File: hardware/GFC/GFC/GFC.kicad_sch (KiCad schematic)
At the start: 11 parts, among them J1 BATCON, J2 Pi Zero/Zero W

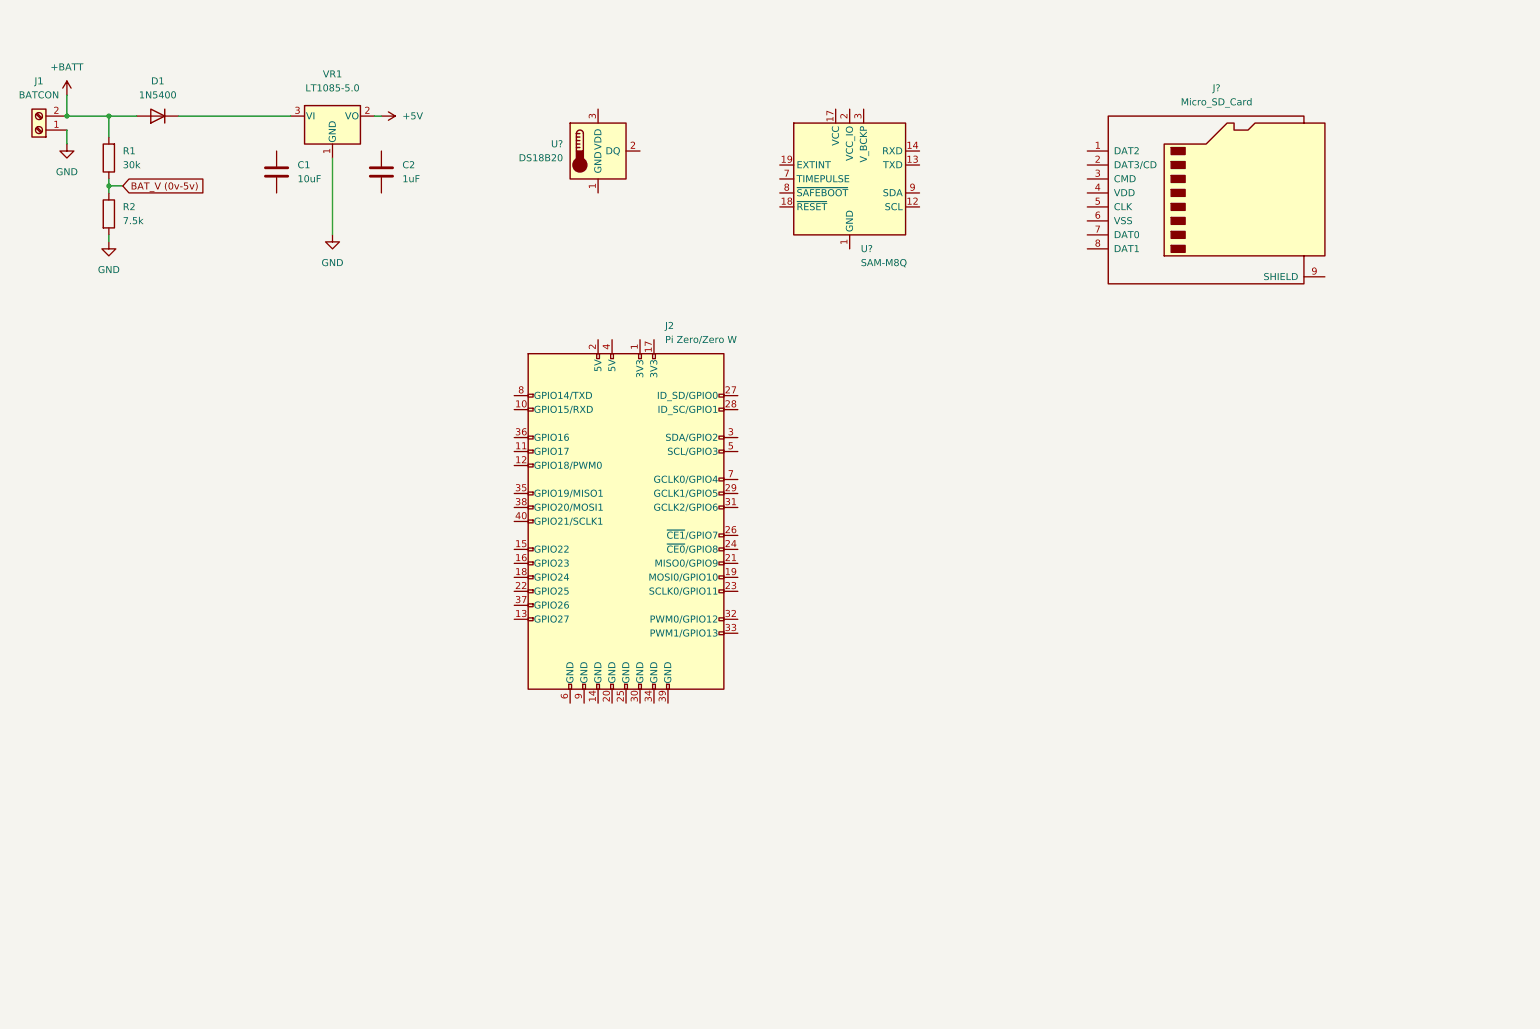
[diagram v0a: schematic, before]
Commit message: Continued work on schematic for GFC. Added BMP390 and DRA818
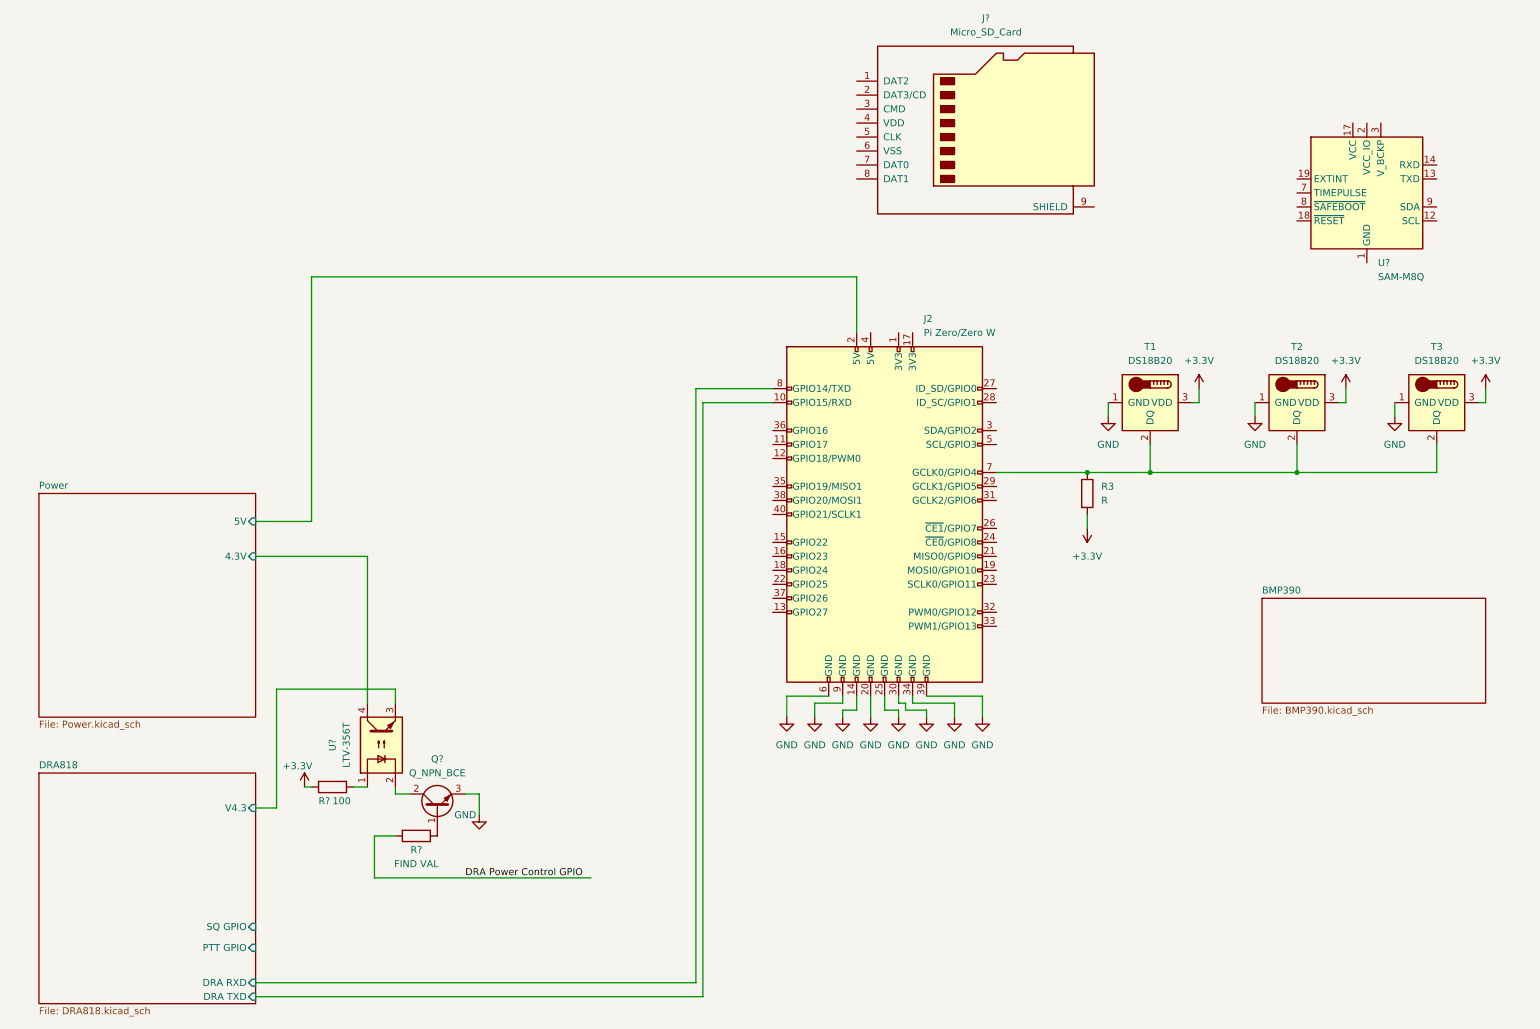
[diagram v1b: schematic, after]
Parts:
- removed C1: 10uF, symbol Device:C
- removed C2: 1uF, symbol Device:C
- removed D1: 1N5400, Diode_THT:D_DO-201AD_P15.24mm_Horizontal, symbol Diode:1N5400
- removed J1: BATCON, symbol Connector:Screw_Terminal_01x02
- removed R1: 30k, symbol Device:R
- removed R2: 7.5k, symbol Device:R
- removed VR1: LT1085-5.0, symbol Regulator_Linear:LT1085-5.0
- added Q?: Q_NPN_BCE, symbol Device:Q_NPN_BCE
- added R3: R, symbol Device:R
- added R?: 100, symbol Device:R
- added R?: FIND VAL, symbol Device:R
- added T2, T3: DS18B20, Package_TO_SOT_THT:TO-92_Inline, symbol Sensor_Temperature:DS18B20
- added U?: LTV-356T, Package_SO:SO-4_4.4x3.6mm_P2.54mm, symbol Isolator:LTV-356T
- gave numbers to parts that had none: 1
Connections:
- net GND: now also J2.14 (GND), J2.20 (GND), J2.25 (GND), J2.30 (GND), J2.34 (GND), J2.39 (GND), J2.6 (GND), J2.9 (GND), T1.1 (GND), Q?.3 (E), T2.1 (GND), T3.1 (GND)
- net at T1.2 (DQ): now also J2.7 (GCLK0/GPIO4), R3.1, T2.2 (DQ), T3.2 (DQ)
- net +3.3V: now reaches T1.3 (VDD)
- net +3.3V: now also R3.2, R?.2, T2.3 (VDD), T3.3 (VDD)
- net DRA818/DRA TXD: now reaches J2.10 (GPIO15/RXD)
- net Power/5V: now reaches J2.2 (5V)
- net DRA818/DRA RXD: now reaches J2.8 (GPIO14/TXD)
- new net: R?.1, U?.1
- new net: Q?.2 (C), U?.2
- new net: Q?.1 (B), R?.1
- new net DRA Power Control GPIO: R?.2
- new net DRA818/V4.3: U?.3
- new net Power/4.3V: U?.4
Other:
- added sheet BMP390 (BMP390.kicad_sch)
- added sheet DRA818 (DRA818.kicad_sch)
- added sheet Power (Power.kicad_sch)
- moved on the sheet: J2, J?, T1, U?

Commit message: Sync board
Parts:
- removed J?: Micro_SD_Card, symbol Connector:Micro_SD_Card
- removed U?: SAM-M8Q, RF_GPS:ublox_SAM-M8Q, symbol RF_GPS:SAM-M8Q
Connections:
- net BMP390 (I2C)/SDA: now reaches J2.3 (SDA/GPIO2)
- net BMP390 (I2C)/SCL: now reaches J2.5 (SCL/GPIO3)
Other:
- sheet BMP390 renamed BMP390 (I2C)
- added sheet SAM-M8Q (SAM-M8Q.kicad_sch)
- sheet BMP390 (I2C) ports: added SCL, SDA, VCC; removed none

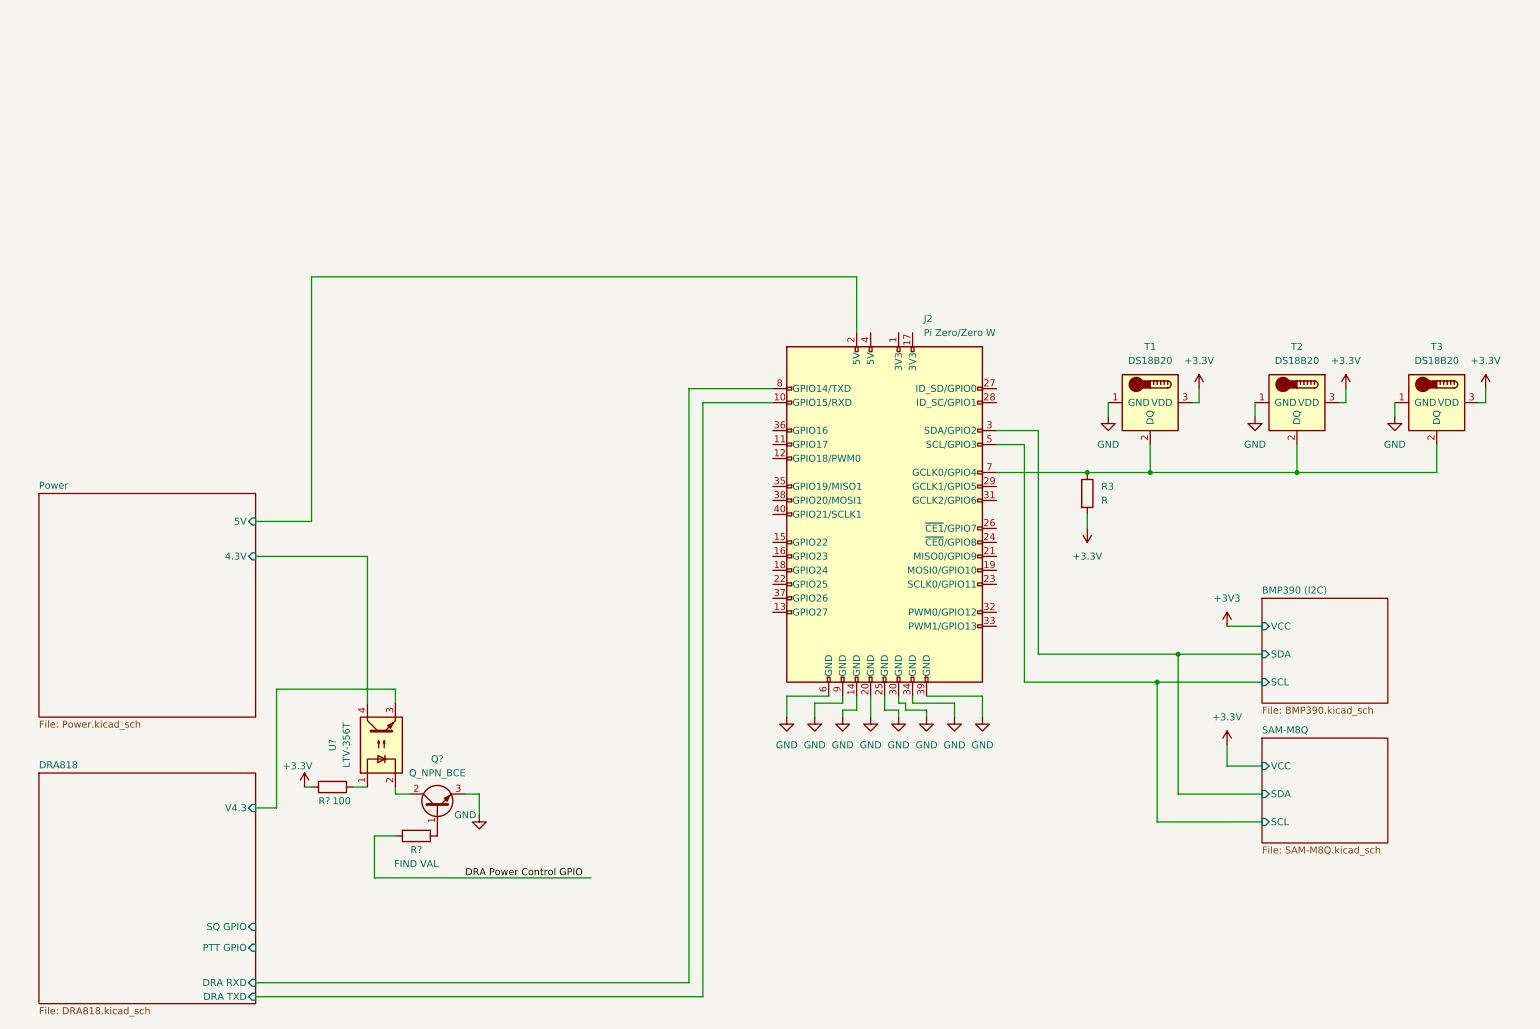
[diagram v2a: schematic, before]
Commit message: Some hardware changes, started to add footprints and part links to digikey. Switching most to SMD
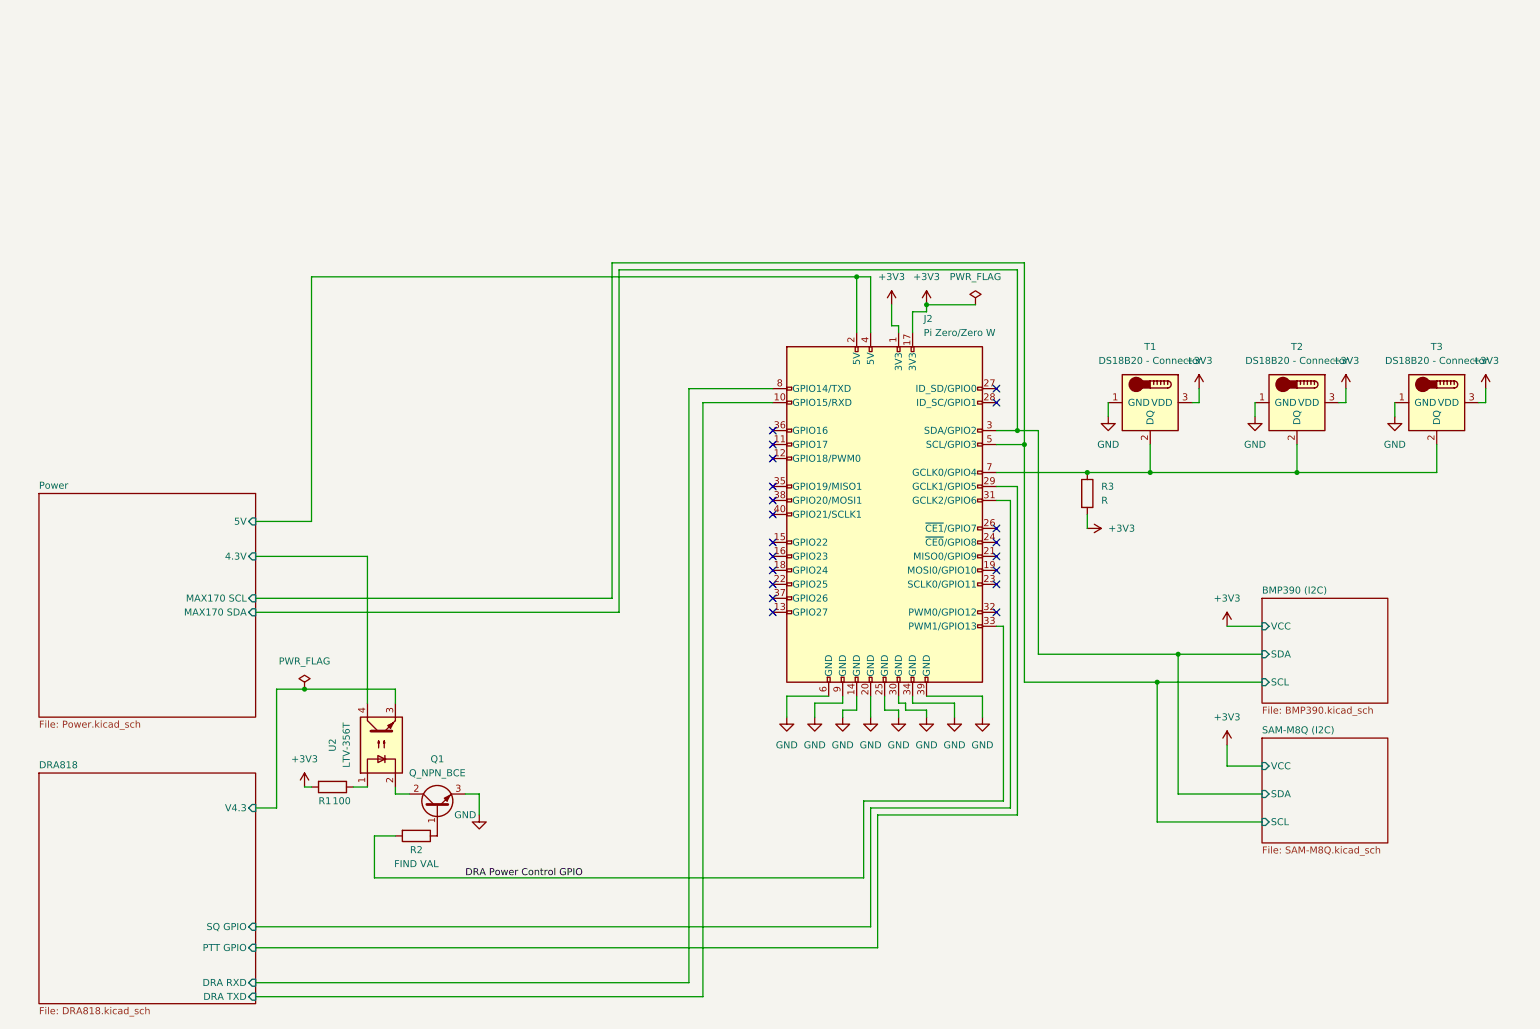
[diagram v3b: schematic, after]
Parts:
- J2: footprint (none) -> N/A; Digikey (none) -> N/A; Unit Price (none) -> 10.00
- T1, T2, T3: value DS18B20 -> DS18B20 - Connector; footprint Package_TO_SOT_THT:TO-92_Inline -> Connector_JST:JST_XH_B3B-XH-AM_1x03_P2.50mm_Vertical; Digikey (none) -> https://www.digikey.com/short/bd73wft8; Unit Price (none) -> 0.18
- U2: renamed from U?; Digikey (none) -> https://www.digikey.com/short/nbv0qj71; Unit Price (none) -> 0.49
- gave numbers to parts that had none: 3
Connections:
- net +3.3V is gone; now on net +3V3: R1.2, R3.2, T1.3 (VDD), T2.3 (VDD), T3.3 (VDD)
- net +3V3: now also J2.1 (3V3), J2.17 (3V3)
- net DRA Power Control GPIO: now also J2.33 (PWM1/GPIO13)
- net DRA818/PTT GPIO: now also J2.29 (GCLK1/GPIO5)
- net DRA818/SQ GPIO: now also J2.31 (GCLK2/GPIO6)
- net Power/5V: now also J2.4 (5V)
- no-connect marks 0 -> 20
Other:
- sheet SAM-M8Q renamed SAM-M8Q (I2C)
- sheet Power ports: added MAX170 SCL, MAX170 SDA; removed none

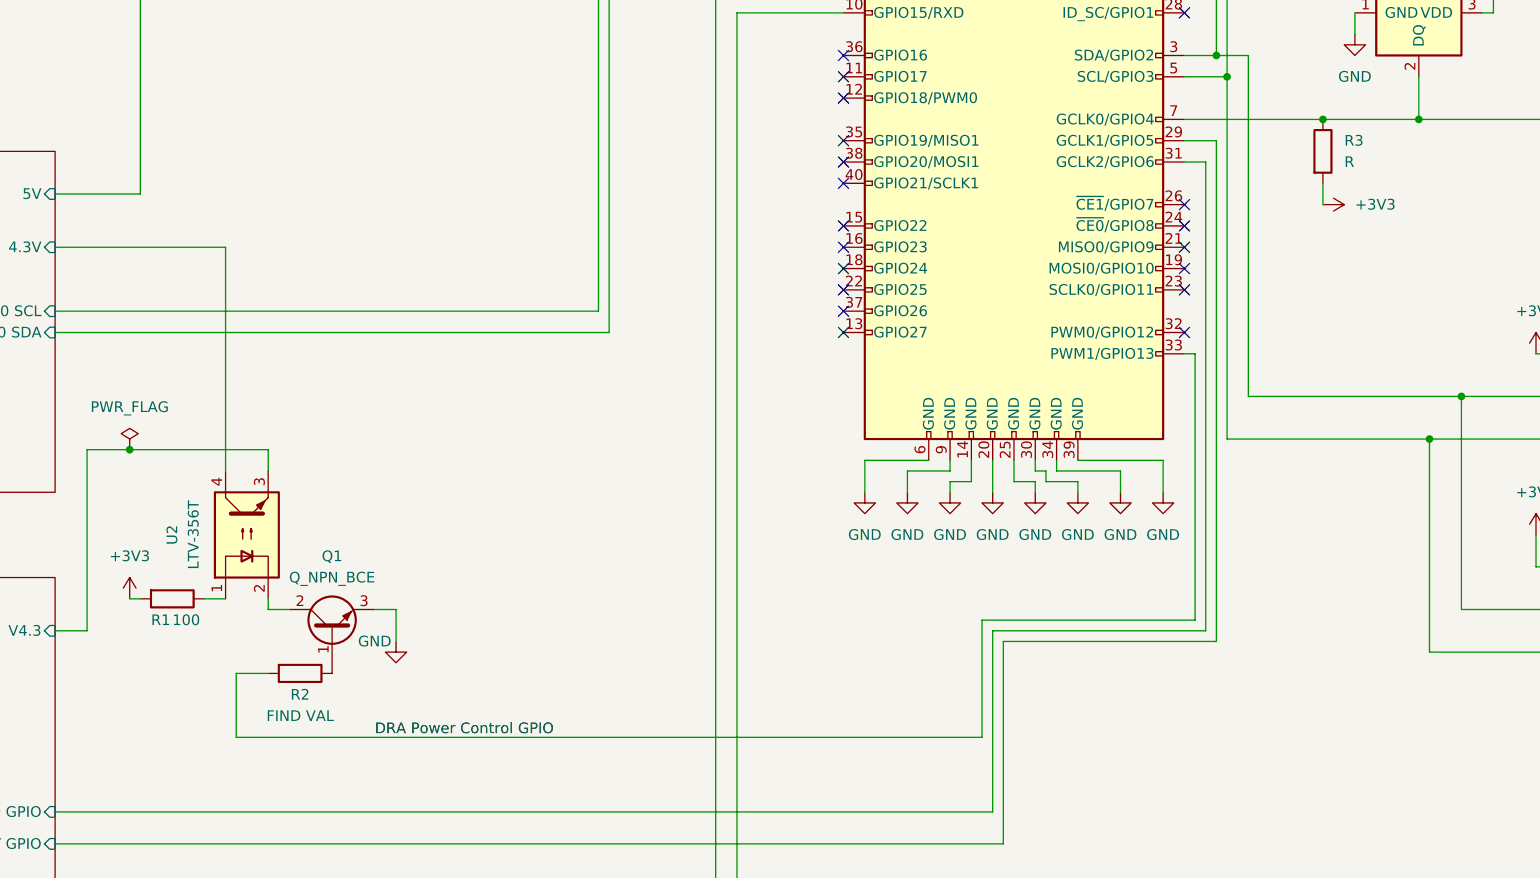
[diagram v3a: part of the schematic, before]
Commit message: Updated footprints - Started work on PCB layout
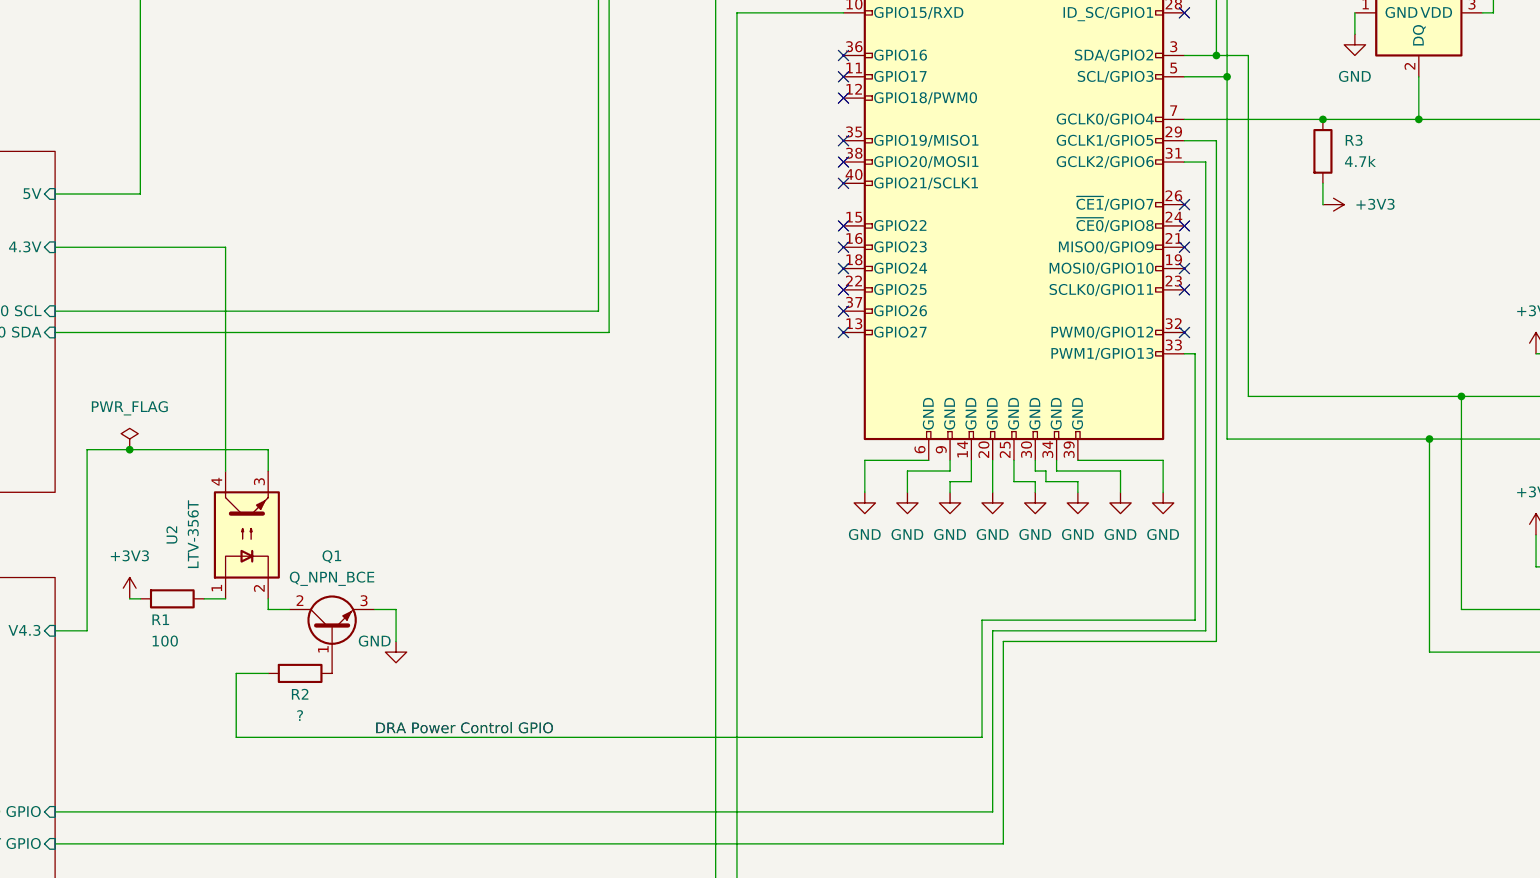
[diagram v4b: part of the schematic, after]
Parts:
- J2: footprint N/A -> Connector_PinSocket_2.54mm:PinSocket_2x20_P2.54mm_Vertical
- Q1: footprint (none) -> Package_TO_SOT_SMD:SOT-23; Digikey (none) -> https://www.digikey.com/short/b477vdt4; Unit Price (none) -> $0.18
- R1: footprint (none) -> Resistor_SMD:R_0805_2012Metric_Pad1.20x1.40mm_HandSolder; Digikey (none) -> https://www.digikey.com/short/j2drdv0p; Unit Price (none) -> 0.10
- R2: value FIND VAL -> ?; footprint (none) -> Resistor_SMD:R_0603_1608Metric_Pad0.98x0.95mm_HandSolder; Digikey (none) -> ?
- R3: value R -> 4.7k; footprint (none) -> Resistor_SMD:R_0603_1608Metric_Pad0.98x0.95mm_HandSolder; Digikey (none) -> https://www.digikey.com/short/m931v8f8; Unit Price (none) -> 0.10
